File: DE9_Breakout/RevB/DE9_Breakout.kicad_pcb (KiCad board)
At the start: 2 copper layers, 19 x 25.4 mm, 3 parts, among them J1 Breakout, J2 DE9 Male, J3 DE9 Female

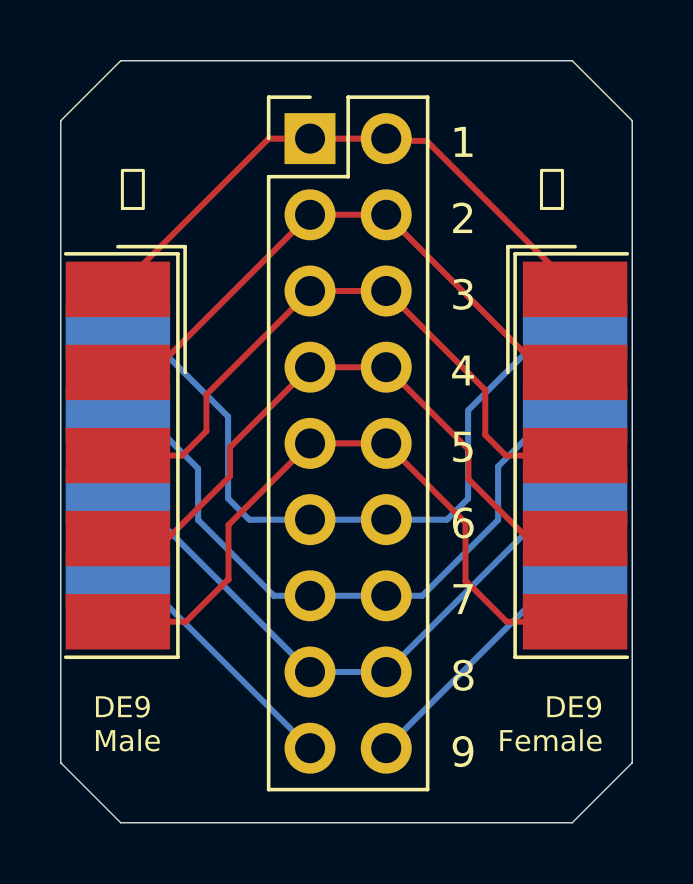
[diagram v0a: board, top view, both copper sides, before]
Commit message: Fixed PCB routing error
Didn't connect pin 9 through, duh
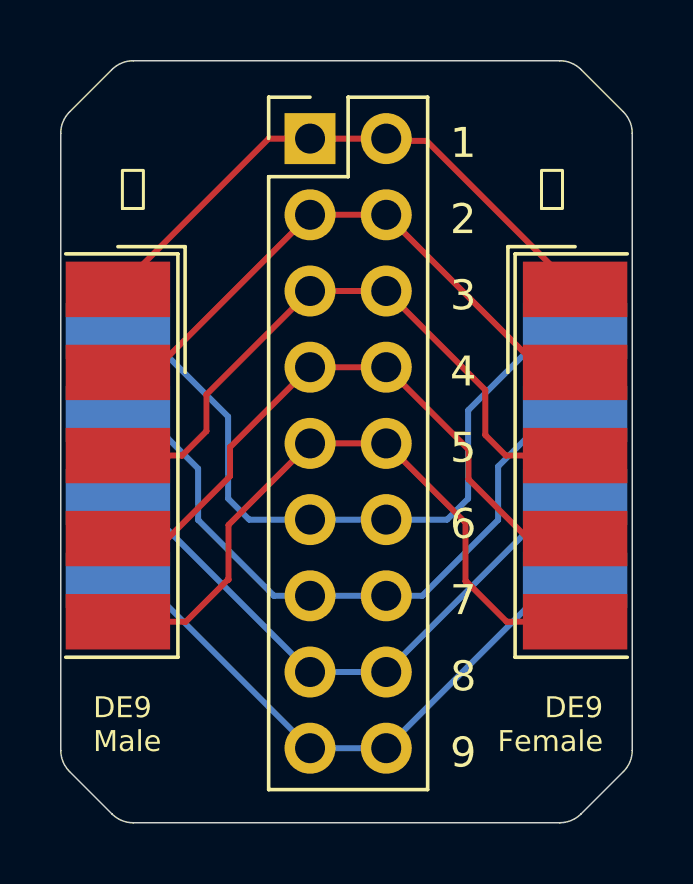
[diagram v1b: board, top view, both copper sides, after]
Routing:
- net /Pin9: track 17.3 -> 19.9 mm
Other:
- outline, holes or cut-outs redrawn
- board text added: "DE9 Breakout, Brett Hallen, Jun 2026"
- board text removed: "DE9 Breakout, Brett Hallen, Jan 2026"
